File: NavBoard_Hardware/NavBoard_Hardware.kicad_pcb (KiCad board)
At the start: 2 copper layers, 61 x 100 mm, 61 parts, among them J1 Conn_Coaxial, Q1 BSS138, Q2 BSS138, U2 ATMEGA328P-Project_Library, U3 OKI, U4 OKI, U5 FGPMMOPA6H, Y1 Crystal

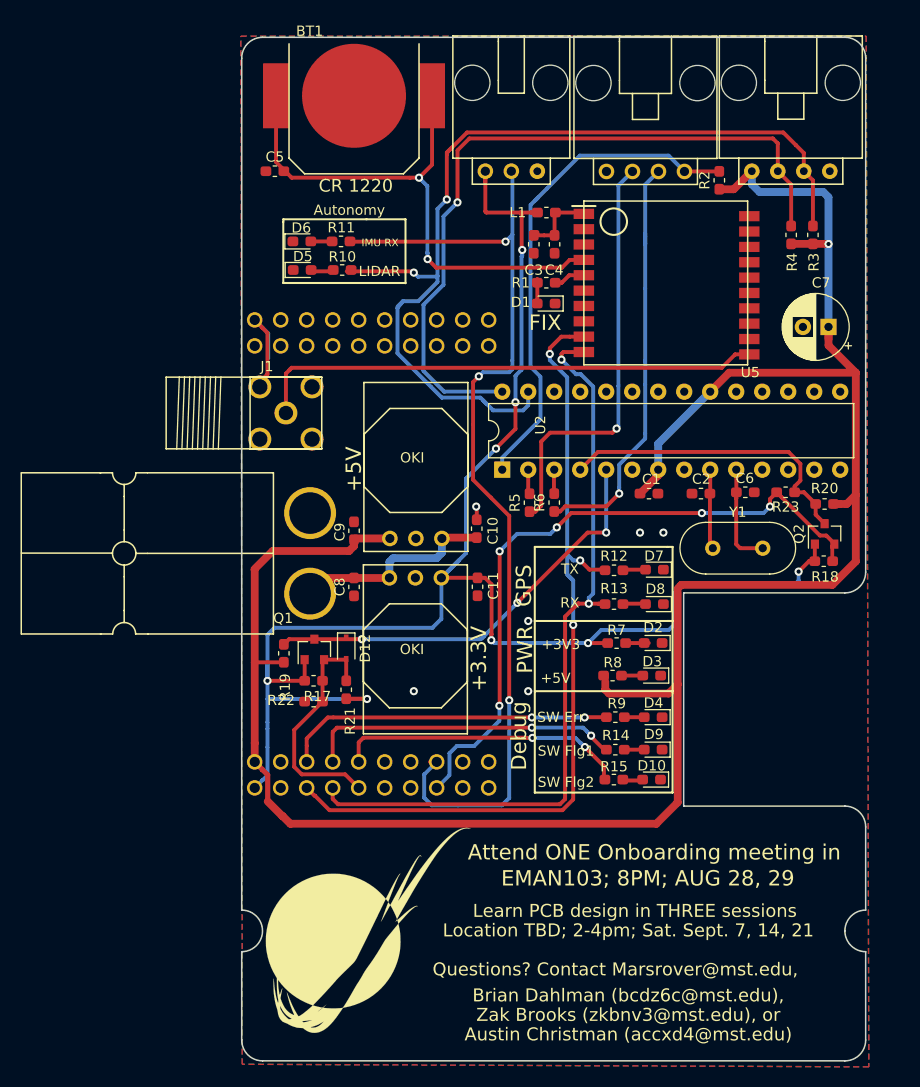
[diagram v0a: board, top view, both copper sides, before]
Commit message: More silkscreen changes
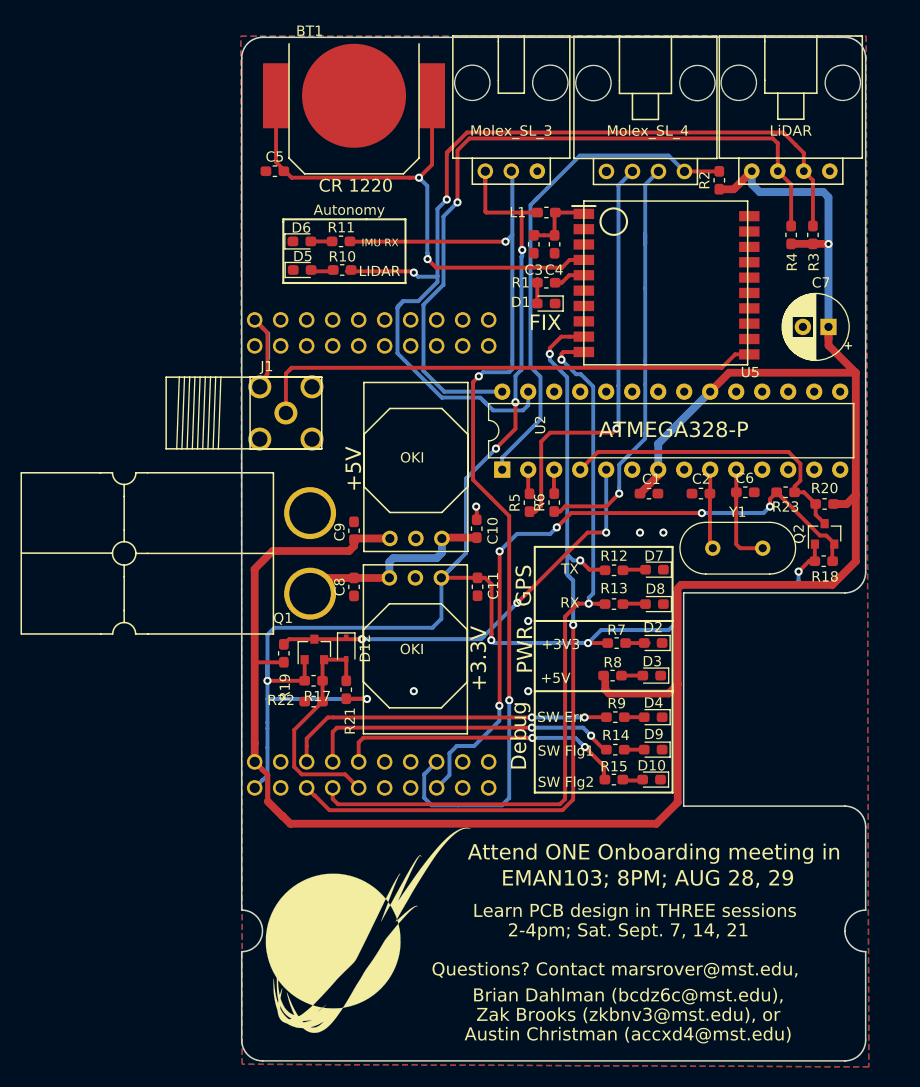
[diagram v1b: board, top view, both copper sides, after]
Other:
- board text added: "2-4pm; Sat. Sept. 7, 14, 21"
- board text added: "ATMEGA328-P"
- board text added: "LiDAR"
- board text added: "Molex_SL_3"
- board text added: "Molex_SL_4"
- board text added: "Questions? Contact marsrover@mst.edu,"
- board text removed: "Location TBD; 2-4pm; Sat. Sept. 7, 14, 21"
- board text removed: "Questions? Contact Marsrover@mst.edu,"
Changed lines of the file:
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@@
   (general
     (thickness 1.6)
-    (drawings 66)
+    (drawings 70)
     (tracks 508)
     (zones 0)
@@
   (page A4)
   (layers
-    (0 F.Cu signal hide)
+    (0 F.Cu signal)
     (31 B.Cu signal)
     (32 B.Adhes user)
@@
       (effects (font (size 1 1) (thickness 0.15)))
     )
-    (fp_text value Molex_SL_04 (at 0.254 -3.7846) (layer F.Fab)
+    (fp_text value Molex_SL_04 (at 0.2312 -3.9624) (layer F.Fab)
       (effects (font (size 1 1) (thickness 0.15)))
     )
@@
       (effects (font (size 1 1) (thickness 0.15)))
     )
-    (fp_text value Battery_Cell (at 0 -8.5344 180) (layer F.Fab)
+    (fp_text value Battery_Cell (at 0 -6.604 180) (layer F.Fab)
       (effects (font (size 1 1) (thickness 0.15)))
     )
@@
       (effects (font (size 1 1) (thickness 0.15)))
     )
-    (fp_text value LiDAR (at 0.254 -3.81) (layer F.Fab)
+    (fp_text value LiDAR (at 0.254 -3.937) (layer F.Fab)
       (effects (font (size 1 1) (thickness 0.15)))
     )
@@
       (effects (font (size 1 1) (thickness 0.15)))
     )
-    (fp_text value Molex_SL_03 (at 0.635 2.032) (layer F.Fab)
+    (fp_text value Molex_SL_03 (at 0 -3.937) (layer F.Fab)
       (effects (font (size 1 1) (thickness 0.15)))
     )
@@
       (xy 12.275375 35.246544) (xy 12.443517 35.256332) (xy 12.564924 35.258447) (xy 12.646643 35.249446)) (layer B.SilkS) (width 0.01))
   )
-  (gr_text "#ROVESOHARD\n" (at 146.05 73.66) (layer B.SilkS)
+  (gr_text LiDAR (at 168.91 61.595) (layer F.SilkS)
+    (effects (font (size 1.016 1.016) (thickness 0.127)))
+  )
+  (gr_text ATMEGA328-P (at 157.48 90.805) (layer F.SilkS)
+    (effects (font (size 1.5 1.5) (thickness 0.3)))
+  )
+  (gr_text Molex_SL_4 (at 154.94 61.595) (layer F.SilkS)
+    (effects (font (size 1.016 1.016) (thickness 0.127)))
+  )
+  (gr_text Molex_SL_3 (at 141.605 61.595) (layer F.SilkS)
+    (effects (font (size 1.016 1.016) (thickness 0.127)))
+  )
+  (gr_text "#ROVESOHARD\n" (at 146.05 74.295) (layer B.SilkS)
     (effects (font (size 3.302 3.302) (thickness 0.381)) (justify mirror))
   )
@@
     (effects (font (size 2.159 2.286) (thickness 0.3)) (justify mirror))
   )
-  (gr_text "MARS ROVER DESIGN TEAM" (at 146.05 61.595) (layer B.SilkS)
+  (gr_text "MARS ROVER DESIGN TEAM" (at 145.415 61.595) (layer B.SilkS)
     (effects (font (size 2.54 2.921) (thickness 0.508)) (justify mirror))
   )
@@
     (effects (font (size 1.27 1.27) (thickness 0.3)))
   )
-  (gr_text "Questions? Contact Marsrover@mst.edu,\n" (at 151.765 143.51) (layer F.SilkS)
+  (gr_text "Questions? Contact marsrover@mst.edu,\n" (at 151.765 143.51) (layer F.SilkS)
     (effects (font (size 1.27 1.27) (thickness 0.3)))
   )
-  (gr_text "Location TBD; 2-4pm; Sat. Sept. 7, 14, 21\n" (at 153.035 139.7) (layer F.SilkS)
+  (gr_text "2-4pm; Sat. Sept. 7, 14, 21\n" (at 153.035 139.7) (layer F.SilkS)
     (effects (font (size 1.27 1.27) (thickness 0.3)))
   )

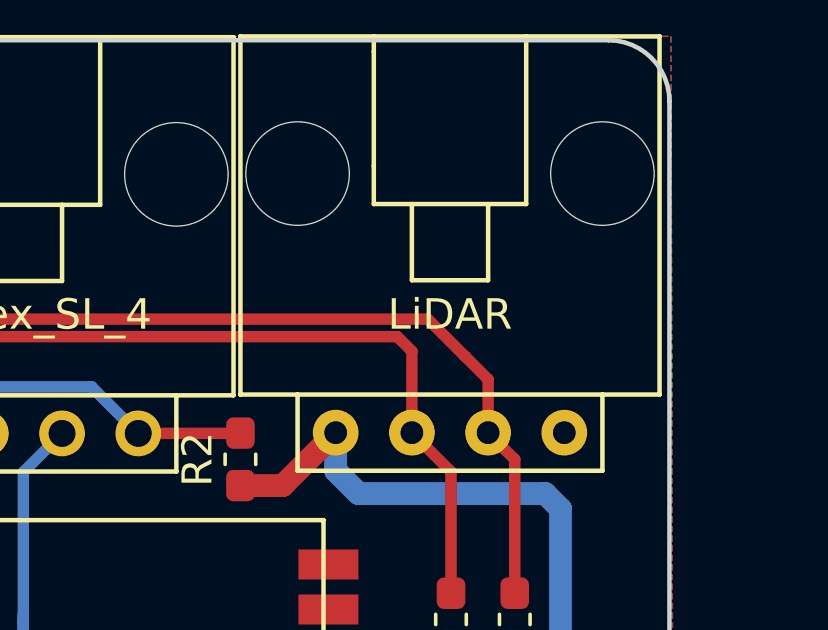
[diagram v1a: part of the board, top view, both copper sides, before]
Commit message: Sleight silkscreen change
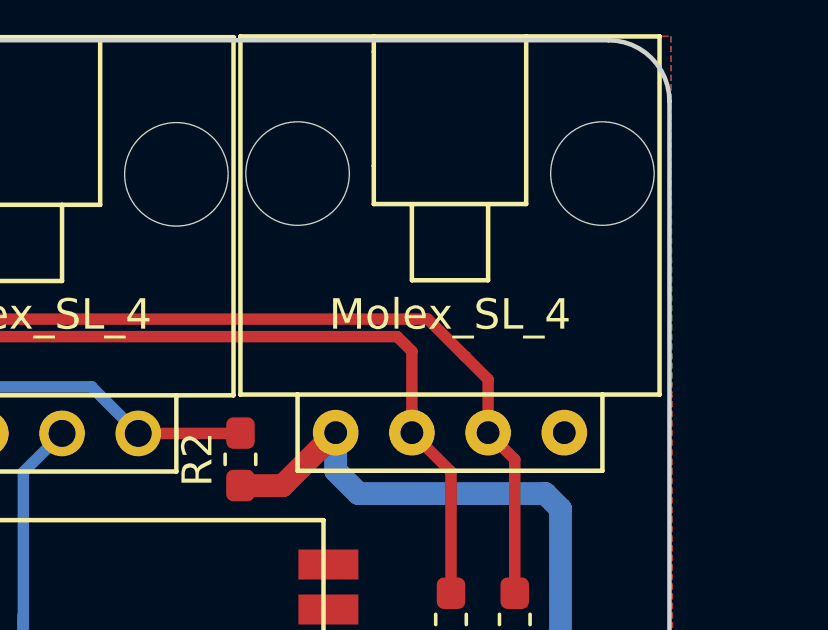
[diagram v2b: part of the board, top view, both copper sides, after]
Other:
- board text removed: "LiDAR"
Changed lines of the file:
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@@
       (xy 12.275375 35.246544) (xy 12.443517 35.256332) (xy 12.564924 35.258447) (xy 12.646643 35.249446)) (layer B.SilkS) (width 0.01))
   )
-  (gr_text LiDAR (at 168.91 61.595) (layer F.SilkS)
+  (gr_text Molex_SL_4 (at 168.91 61.595) (layer F.SilkS)
     (effects (font (size 1.016 1.016) (thickness 0.127)))
   )

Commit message: Changed Dahls email
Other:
- board text added: "Brian Dahlman (bdahlman@mst.edu),"
- board text removed: "Brian Dahlman (bcdz6c@mst.edu),"
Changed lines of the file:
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@@
     (effects (font (size 1.27 1.27) (thickness 0.3)))
   )
-  (gr_text "Brian Dahlman (bcdz6c@mst.edu), \n" (at 153.035 146.05) (layer F.SilkS)
+  (gr_text "Brian Dahlman (bdahlman@mst.edu), \n" (at 153.035 146.05) (layer F.SilkS)
     (effects (font (size 1.27 1.27) (thickness 0.3)))
   )

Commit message: small updates
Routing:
- net +5V: vias 1 -> 3
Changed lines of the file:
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@@
-(kicad_pcb (version 20171130) (host pcbnew "(5.0.0)")
+(kicad_pcb (version 20171130) (host pcbnew "(5.1.2)-1")
   (general
     (thickness 1.6)
     (drawings 70)
-    (tracks 508)
+    (tracks 512)
     (zones 0)
     (modules 61)
@@
   )
   (setup
-    (last_trace_width 0.25)
+    (last_trace_width 0.508)
     (user_trace_width 0.381)
     (user_trace_width 0.508)
@@
     (zone_45_only no)
     (trace_min 0.2)
-    (segment_width 0.2)
-    (edge_width 0.15)
     (via_size 0.8)
     (via_drill 0.4)
@@
     (uvia_min_size 0.2)
     (uvia_min_drill 0.1)
+    (edge_width 0.15)
+    (segment_width 0.2)
     (pcb_text_width 0.3)
     (pcb_text_size 1.5 1.5)
@@
       (drillshape 0)
       (scaleselection 1)
-      (outputdirectory "../Documentation/Gerbs/"))
+      (outputdirectory "./"))
   )
   (net 0 "")
@@
   (segment (start 116.5352 121.412) (end 116.5352 123.2408) (width 0.762) (layer F.Cu) (net 7))
   (segment (start 157.8584 127.2032) (end 157.8584 115.6716) (width 0.762) (layer F.Cu) (net 7))
-  (segment (start 155.7756 129.286) (end 157.8584 127.2032) (width 0.762) (layer F.Cu) (net 7))
-  (segment (start 120.015 129.286) (end 155.7756 129.286) (width 0.762) (layer F.Cu) (net 7))
+  (segment (start 155.7756 129.286) (end 155.7756 129.286) (width 0.762) (layer F.Cu) (net 7))
+  (segment (start 120.015 129.286) (end 120.142 129.286) (width 0.762) (layer F.Cu) (net 7))
   (segment (start 119.272019 128.543019) (end 120.015 129.286) (width 0.762) (layer F.Cu) (net 7))
   (segment (start 117.8026 127.1016) (end 119.244019 128.543019) (width 0.762) (layer F.Cu) (net 7))
@@
   (segment (start 155.956 95.25) (end 154.178 97.028) (width 0.762) (layer F.Cu) (net 7))
   (segment (start 155.956 94.6912) (end 155.956 95.25) (width 0.762) (layer F.Cu) (net 7))
+  (segment (start 155.7756 129.286) (end 157.8584 127.2032) (width 0.762) (layer F.Cu) (net 7))
+  (via (at 155.7756 129.286) (size 0.8) (drill 0.4) (layers F.Cu B.Cu) (net 7))
+  (via (at 120.142 129.286) (size 0.8) (drill 0.4) (layers F.Cu B.Cu) (net 7))
+  (segment (start 120.142 129.286) (end 155.7756 129.286) (width 0.508) (layer B.Cu) (net 7))
   (segment (start 136.3472 68.58) (end 136.3726 68.5546) (width 0.381) (layer B.Cu) (net 8))
   (segment (start 167.673606 65.565606) (end 167.64 65.532) (width 0.381) (layer F.Cu) (net 8))
